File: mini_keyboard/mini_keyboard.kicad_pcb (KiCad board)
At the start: 2 copper layers, 158.8 x 114.3 mm, 46 parts, among them U1 MX1A-11NN, U10 MX1A-11NN, U100 DEV-15583, U101 ABX00027, U11 MX1A-11NN, U12 MX1A-11NN, U13 MX1A-11NN, U14 MX1A-11NN, U15 MX1A-11NN, U16 MX1A-11NN, U17 MX1A-11NN, U18 MX1A-11NN, U19 MX1A-11NN, U2 MX1A-11NN, U20 MX1A-11NN, U21 MX1A-11NN, U22 MX1A-11NN, U23 MX1A-11NN, U24 MX1A-11NN, U25 MX1A-11NN, U26 MX1A-11NN, U27 MX1A-11NN, U29 MX1A-11NN, U3 MX1A-11NN, U30 MX1A-11NN, U31 MX1A-11NN, U32 MX1A-11NN, U33 MX1A-11NN, U34 MX1A-11NN, U36 MX1A-11NN, U37 MX1A-11NN, U38 MX1A-11NN, U39 MX1A-11NN, U4 MX1A-11NN, U5 MX1A-11NN, U6 MX1A-11NN, U7 MX1A-11NN, U8 MX1A-11NN, U9 MX1A-11NN

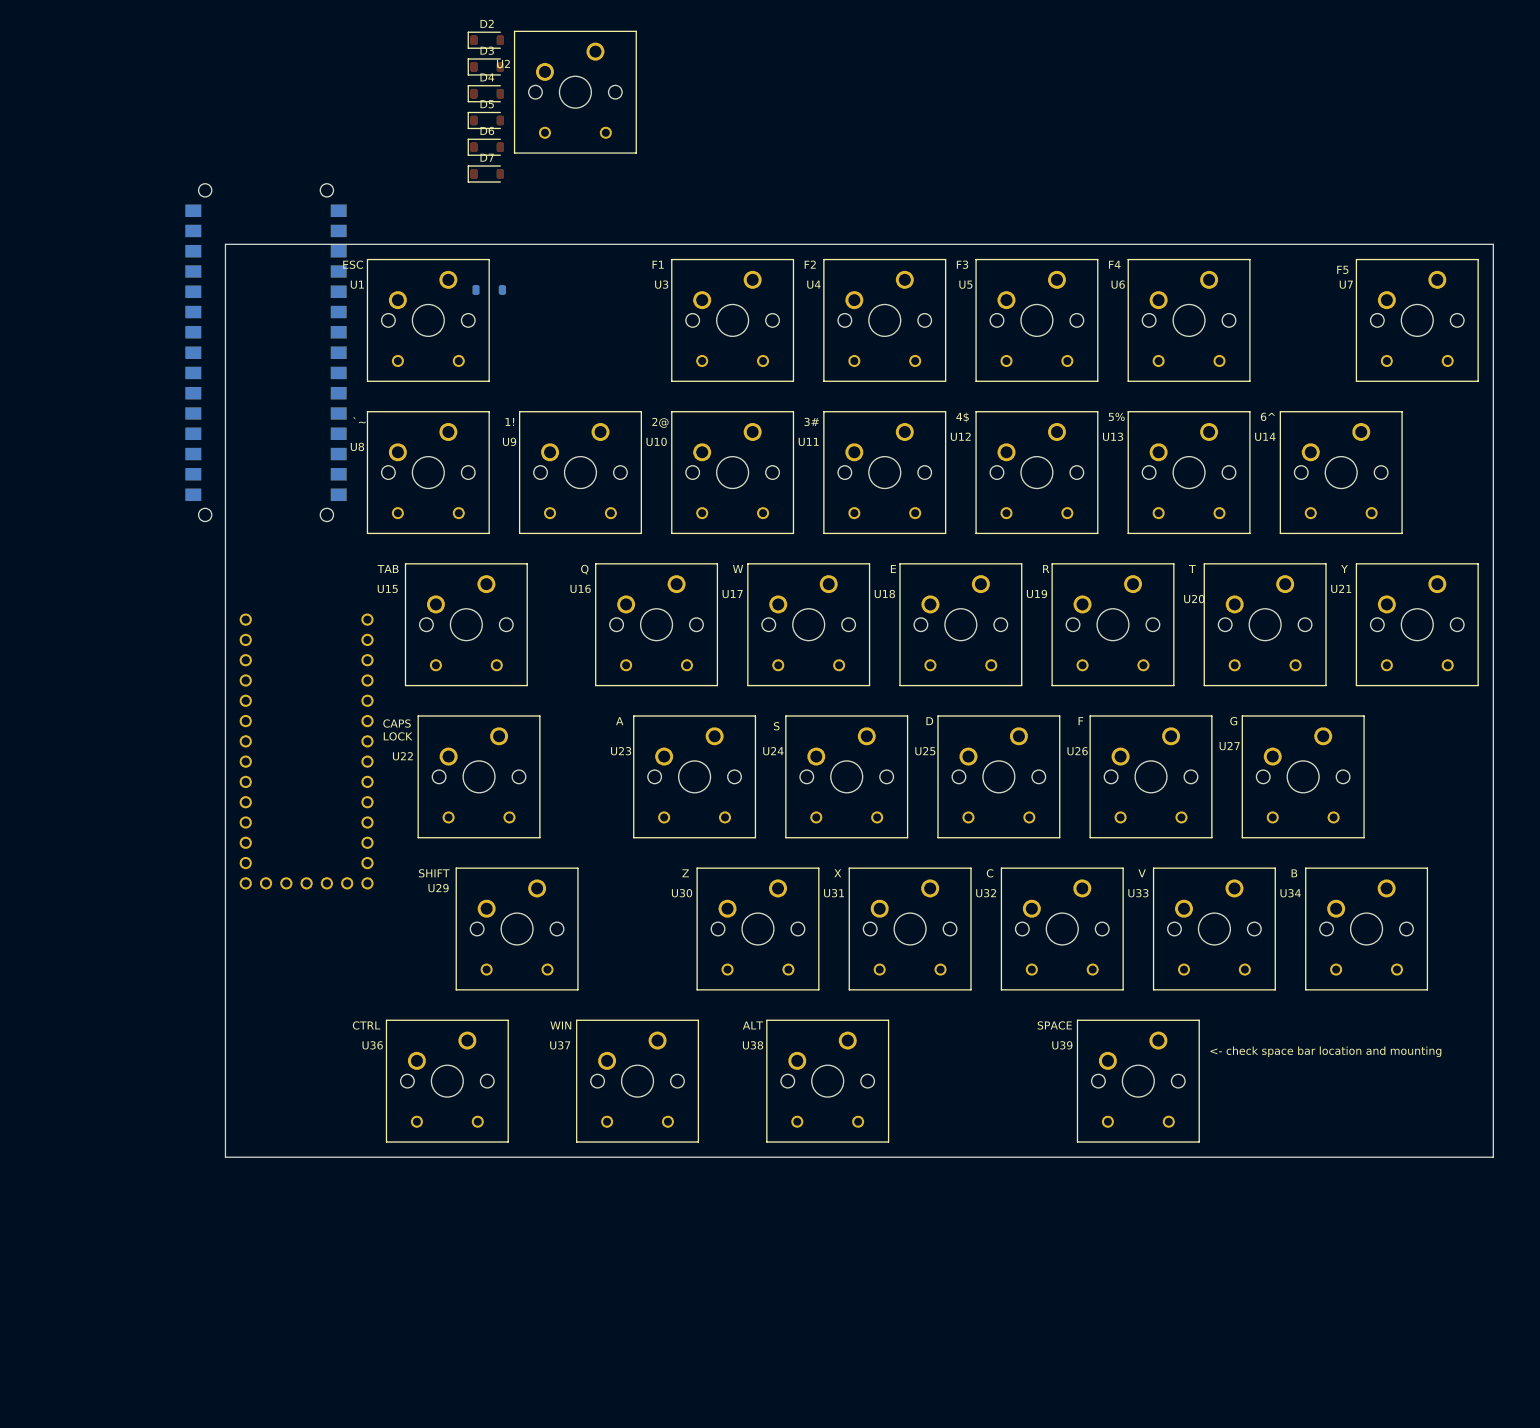
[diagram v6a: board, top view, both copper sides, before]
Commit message: initial placement of all diodes
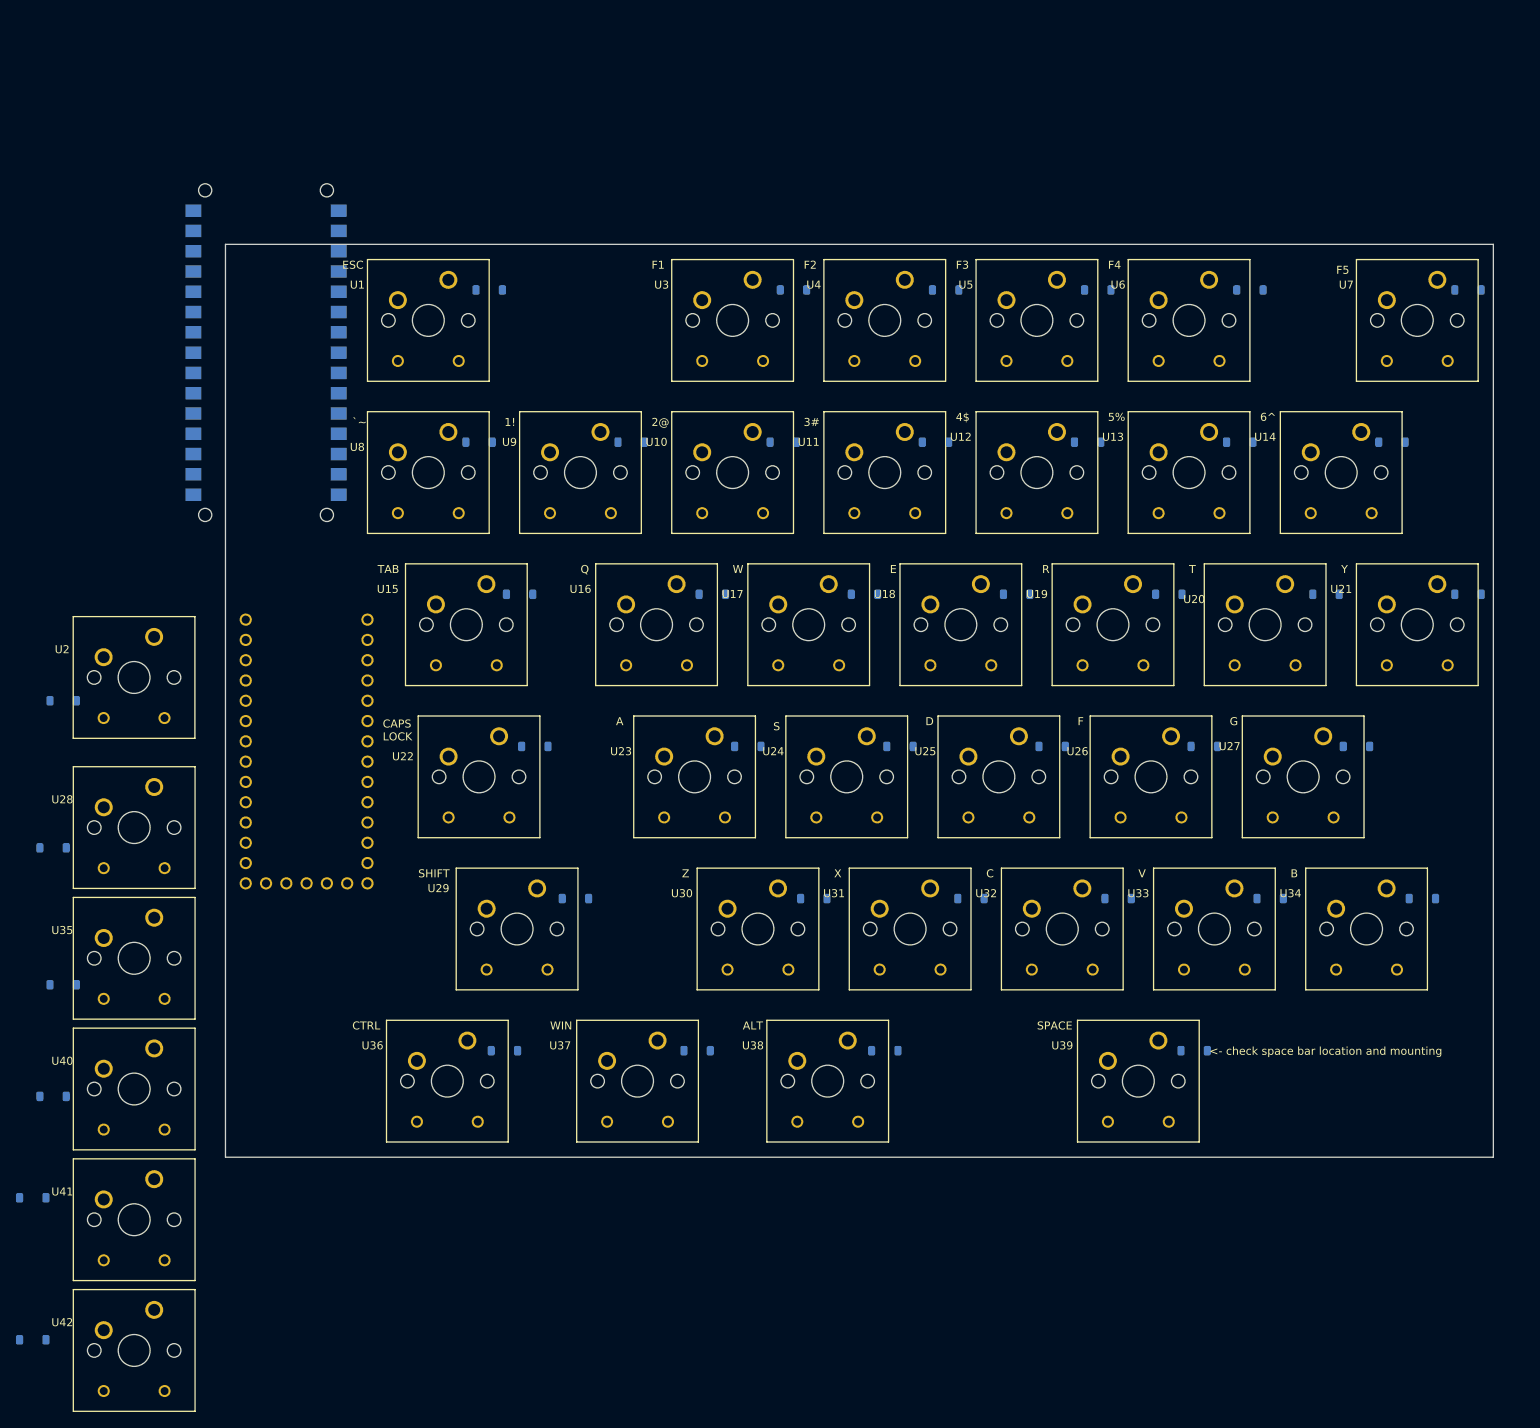
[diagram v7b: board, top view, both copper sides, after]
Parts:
- added D10: 1N4148W, Diode_SMD:D_SOD-123, B.Cu at (95.2, 50.2)
- added D11: 1N4148W, Diode_SMD:D_SOD-123, B.Cu at (114.3, 50.2)
- added D12: 1N4148W, Diode_SMD:D_SOD-123, B.Cu at (133.3, 50.2)
- added D13: 1N4148W, Diode_SMD:D_SOD-123, B.Cu at (152.4, 50.2)
- added D14: 1N4148W, Diode_SMD:D_SOD-123, B.Cu at (171.4, 50.2)
- added D15: 1N4148W, Diode_SMD:D_SOD-123, B.Cu at (62.2, 69.2)
- added D16: 1N4148W, Diode_SMD:D_SOD-123, B.Cu at (86.4, 69.2)
- added D17: 1N4148W, Diode_SMD:D_SOD-123, B.Cu at (105.4, 69.2)
- added D18: 1N4148W, Diode_SMD:D_SOD-123, B.Cu at (124.5, 69.2)
- added D19: 1N4148W, Diode_SMD:D_SOD-123, B.Cu at (143.5, 69.2)
- added D20: 1N4148W, Diode_SMD:D_SOD-123, B.Cu at (163.2, 69.2)
- added D21: 1N4148W, Diode_SMD:D_SOD-123, B.Cu at (181.0, 69.2)
- added D22: 1N4148W, Diode_SMD:D_SOD-123, B.Cu at (64.1, 88.3)
- added D23: 1N4148W, Diode_SMD:D_SOD-123, B.Cu at (90.8, 88.3)
- added D24: 1N4148W, Diode_SMD:D_SOD-123, B.Cu at (109.9, 88.3)
- added D25: 1N4148W, Diode_SMD:D_SOD-123, B.Cu at (128.9, 88.3)
- added D26: 1N4148W, Diode_SMD:D_SOD-123, B.Cu at (148.0, 88.3)
- added D27: 1N4148W, Diode_SMD:D_SOD-123, B.Cu at (167.0, 88.3)
- added D28: 1N4148W, Diode_SMD:D_SOD-123, B.Cu at (3.81, 101.0)
- added D29: 1N4148W, Diode_SMD:D_SOD-123, B.Cu at (69.2, 107.3)
- added D30: 1N4148W, Diode_SMD:D_SOD-123, B.Cu at (99.1, 107.3)
- added D31: 1N4148W, Diode_SMD:D_SOD-123, B.Cu at (118.7, 107.3)
- added D32: 1N4148W, Diode_SMD:D_SOD-123, B.Cu at (137.2, 107.3)
- added D33: 1N4148W, Diode_SMD:D_SOD-123, B.Cu at (156.2, 107.3)
- added D34: 1N4148W, Diode_SMD:D_SOD-123, B.Cu at (175.3, 107.3)
- added D35: 1N4148W, Diode_SMD:D_SOD-123, B.Cu at (5.08, 118.1)
- added D36: 1N4148W, Diode_SMD:D_SOD-123, B.Cu at (60.3, 126.4)
- added D37: 1N4148W, Diode_SMD:D_SOD-123, B.Cu at (84.5, 126.4)
- added D38: 1N4148W, Diode_SMD:D_SOD-123, B.Cu at (108.0, 126.4)
- added D39: 1N4148W, Diode_SMD:D_SOD-123, B.Cu at (146.7, 126.4)
- added D40: 1N4148W, Diode_SMD:D_SOD-123, B.Cu at (3.81, 132.1)
- added D41: 1N4148W, Diode_SMD:D_SOD-123, B.Cu at (1.27, 144.8)
- added D42: 1N4148W, Diode_SMD:D_SOD-123, B.Cu at (1.27, 162.6)
- added D8: 1N4148W, Diode_SMD:D_SOD-123, B.Cu at (57.1, 50.2)
- added D9: 1N4148W, Diode_SMD:D_SOD-123, B.Cu at (76.2, 50.2)
- added U28: MX1A-11NN, pedrolib:CHERRY_MX1A-11NN_SWITCH, F.Cu at (14.0, 98.4)
- added U35: MX1A-11NN, pedrolib:CHERRY_MX1A-11NN_SWITCH, F.Cu at (14.0, 114.8)
- added U40: MX1A-11NN, pedrolib:CHERRY_MX1A-11NN_SWITCH, F.Cu at (14.0, 131.2)
- added U41: MX1A-11NN, pedrolib:CHERRY_MX1A-11NN_SWITCH, F.Cu at (14.0, 147.5)
- added U42: MX1A-11NN, pedrolib:CHERRY_MX1A-11NN_SWITCH, F.Cu at (14.0, 163.9)
- D2, D3, D4, D5, D6, D7: moved to B.Cu
- moved D7 123.7 mm to (181.0, 31.1), turned to 180 degrees
- moved D2 98.3 mm to (5.08, 82.5), turned to 180 degrees
- moved D6 97.2 mm to (153.7, 31.1), turned to 180 degrees
- moved U2 91.8 mm to (14.0, 79.6)
- moved D5 79.3 mm to (134.6, 31.1), turned to 180 degrees
- moved D4 62.4 mm to (115.6, 31.1), turned to 180 degrees
- moved D3 47.4 mm to (96.5, 31.1), turned to 180 degrees
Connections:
- D1 pad 1: unconnected-(D1-K-Pad1) -> /row0
- D2 pad 1: unconnected-(D2-K-Pad1) -> /row0
- D2 pad 2: unconnected-(D2-A-Pad2) -> Net-(D2-A)
- D3 pad 1: unconnected-(D3-K-Pad1) -> /row0
- D3 pad 2: unconnected-(D3-A-Pad2) -> Net-(D3-A)
- D4 pad 1: unconnected-(D4-K-Pad1) -> /row0
- D4 pad 2: unconnected-(D4-A-Pad2) -> Net-(D4-A)
- D5 pad 1: unconnected-(D5-K-Pad1) -> /row0
- D5 pad 2: unconnected-(D5-A-Pad2) -> Net-(D5-A)
- D6 pad 1: unconnected-(D6-K-Pad1) -> /row0
- D6 pad 2: unconnected-(D6-A-Pad2) -> Net-(D6-A)
- D7 pad 1: unconnected-(D7-K-Pad1) -> /row0
- D7 pad 2: unconnected-(D7-A-Pad2) -> Net-(D7-A)
- U1 pad P$2: unconnected-(U1-PadP$2) -> /col0
- U10 pad P$1: unconnected-(U10-PadP$1) -> Net-(D10-A)
- U10 pad P$2: unconnected-(U10-PadP$2) -> /col2
- U11 pad P$1: unconnected-(U11-PadP$1) -> Net-(D11-A)
- U11 pad P$2: unconnected-(U11-PadP$2) -> /col3
- U12 pad P$1: unconnected-(U12-PadP$1) -> Net-(D12-A)
- U12 pad P$2: unconnected-(U12-PadP$2) -> /col4
- U13 pad P$1: unconnected-(U13-PadP$1) -> Net-(D13-A)
- U13 pad P$2: unconnected-(U13-PadP$2) -> /col5
- U14 pad P$1: unconnected-(U14-PadP$1) -> Net-(D14-A)
- U14 pad P$2: unconnected-(U14-PadP$2) -> /col6
- U15 pad P$1: unconnected-(U15-PadP$1) -> Net-(D15-A)
- U15 pad P$2: unconnected-(U15-PadP$2) -> /col0
- U16 pad P$1: unconnected-(U16-PadP$1) -> Net-(D16-A)
- U16 pad P$2: unconnected-(U16-PadP$2) -> /col1
- U17 pad P$1: unconnected-(U17-PadP$1) -> Net-(D17-A)
- U17 pad P$2: unconnected-(U17-PadP$2) -> /col2
- U18 pad P$1: unconnected-(U18-PadP$1) -> Net-(D18-A)
- U18 pad P$2: unconnected-(U18-PadP$2) -> /col3
- U19 pad P$1: unconnected-(U19-PadP$1) -> Net-(D19-A)
- U19 pad P$2: unconnected-(U19-PadP$2) -> /col4
- U2 pad P$1: unconnected-(U2-PadP$1) -> Net-(D2-A)
- U2 pad P$2: unconnected-(U2-PadP$2) -> /col1
- U20 pad P$1: unconnected-(U20-PadP$1) -> Net-(D20-A)
- U20 pad P$2: unconnected-(U20-PadP$2) -> /col5
- U21 pad P$1: unconnected-(U21-PadP$1) -> Net-(D21-A)
- U21 pad P$2: unconnected-(U21-PadP$2) -> /col6
- U22 pad P$1: unconnected-(U22-PadP$1) -> Net-(D22-A)
- U22 pad P$2: unconnected-(U22-PadP$2) -> /col0
- U23 pad P$1: unconnected-(U23-PadP$1) -> Net-(D23-A)
- U23 pad P$2: unconnected-(U23-PadP$2) -> /col1
- U24 pad P$1: unconnected-(U24-PadP$1) -> Net-(D24-A)
- U24 pad P$2: unconnected-(U24-PadP$2) -> /col2
- U25 pad P$1: unconnected-(U25-PadP$1) -> Net-(D25-A)
- U25 pad P$2: unconnected-(U25-PadP$2) -> /col3
- U26 pad P$1: unconnected-(U26-PadP$1) -> Net-(D26-A)
- U26 pad P$2: unconnected-(U26-PadP$2) -> /col4
- U27 pad P$1: unconnected-(U27-PadP$1) -> Net-(D27-A)
- U27 pad P$2: unconnected-(U27-PadP$2) -> /col5
- U29 pad P$1: unconnected-(U29-PadP$1) -> Net-(D29-A)
- U29 pad P$2: unconnected-(U29-PadP$2) -> /col0
- U3 pad P$1: unconnected-(U3-PadP$1) -> Net-(D3-A)
- U3 pad P$2: unconnected-(U3-PadP$2) -> /col2
- U30 pad P$1: unconnected-(U30-PadP$1) -> Net-(D30-A)
- U30 pad P$2: unconnected-(U30-PadP$2) -> /col1
- U31 pad P$1: unconnected-(U31-PadP$1) -> Net-(D31-A)
- U31 pad P$2: unconnected-(U31-PadP$2) -> /col2
- U32 pad P$1: unconnected-(U32-PadP$1) -> Net-(D32-A)
- U32 pad P$2: unconnected-(U32-PadP$2) -> /col3
- U33 pad P$1: unconnected-(U33-PadP$1) -> Net-(D33-A)
- U33 pad P$2: unconnected-(U33-PadP$2) -> /col4
- U34 pad P$1: unconnected-(U34-PadP$1) -> Net-(D34-A)
- U34 pad P$2: unconnected-(U34-PadP$2) -> /col5
- U36 pad P$1: unconnected-(U36-PadP$1) -> Net-(D36-A)
- U36 pad P$2: unconnected-(U36-PadP$2) -> /col0
- U37 pad P$1: unconnected-(U37-PadP$1) -> Net-(D37-A)
- U37 pad P$2: unconnected-(U37-PadP$2) -> /col1
- U38 pad P$1: unconnected-(U38-PadP$1) -> Net-(D38-A)
- U38 pad P$2: unconnected-(U38-PadP$2) -> /col2
- U39 pad P$1: unconnected-(U39-PadP$1) -> Net-(D39-A)
- U39 pad P$2: unconnected-(U39-PadP$2) -> /col3
- U4 pad P$1: unconnected-(U4-PadP$1) -> Net-(D4-A)
- U4 pad P$2: unconnected-(U4-PadP$2) -> /col3
- U5 pad P$1: unconnected-(U5-PadP$1) -> Net-(D5-A)
- U5 pad P$2: unconnected-(U5-PadP$2) -> /col4
- U6 pad P$1: unconnected-(U6-PadP$1) -> Net-(D6-A)
- U6 pad P$2: unconnected-(U6-PadP$2) -> /col5
- U7 pad P$1: unconnected-(U7-PadP$1) -> Net-(D7-A)
- U7 pad P$2: unconnected-(U7-PadP$2) -> /col6
- U8 pad P$1: unconnected-(U8-PadP$1) -> Net-(D8-A)
- U8 pad P$2: unconnected-(U8-PadP$2) -> /col0
- U9 pad P$1: unconnected-(U9-PadP$1) -> Net-(D9-A)
- U9 pad P$2: unconnected-(U9-PadP$2) -> /col1
